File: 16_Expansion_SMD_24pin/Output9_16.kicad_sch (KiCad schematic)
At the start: 20 parts, among them J10 String10, J11 String11, J12 String12, J13 String13, J14 String14, J15 String15, J16 String16, J9 String9, U2 74HC245

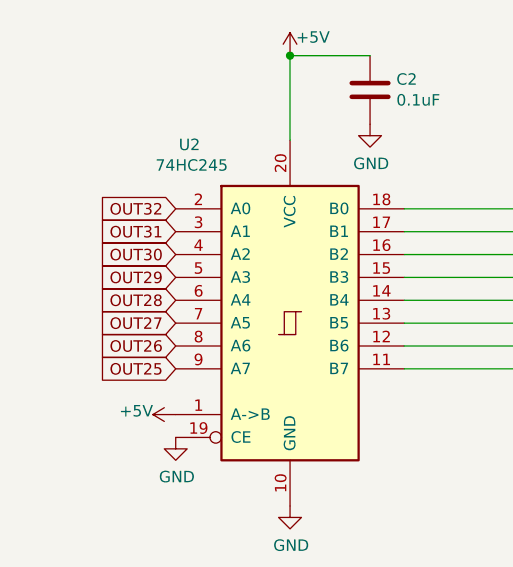
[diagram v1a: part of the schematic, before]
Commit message: added buffer resistors
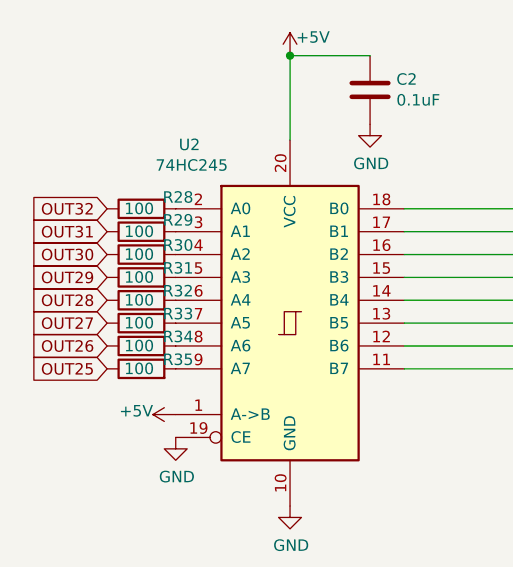
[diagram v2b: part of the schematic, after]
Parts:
- added R28, R29, R30, R31, R32, R33, R34, R35: 100, Resistor_SMD:R_0603_1608Metric_Pad0.98x0.95mm_HandSolder, symbol Device:R
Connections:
- net OUT25: now also R35.1; no longer U2.9 (A7)
- net OUT26: now also R34.1; no longer U2.8 (A6)
- net OUT27: now also R33.1; no longer U2.7 (A5)
- net OUT28: now also R32.1; no longer U2.6 (A4)
- net OUT29: now also R31.1; no longer U2.5 (A3)
- net OUT30: now also R30.1; no longer U2.4 (A2)
- net OUT31: now also R29.1; no longer U2.3 (A1)
- net OUT32: now also R28.1; no longer U2.2 (A0)
- new net: R28.2, U2.2 (A0)
- new net: R29.2, U2.3 (A1)
- new net: R30.2, U2.4 (A2)
- new net: R31.2, U2.5 (A3)
- new net: R32.2, U2.6 (A4)
- new net: R33.2, U2.7 (A5)
- new net: R34.2, U2.8 (A6)
- new net: R35.2, U2.9 (A7)
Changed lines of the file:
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@@
   (title_block
     (title "16 Expansion SMD 24pin")
-    (date "2022-06-05")
-    (rev "v2")
+    (date "2022-08-12")
+    (rev "v3")
     (company "Scott Hanson")
   )
@@
     (effects (font (size 1.27 1.27)) (justify left bottom))
   )
-  (global_label "OUT26" (shape input) (at 117.602 124.968 180) (fields_autoplaced)
+  (global_label "OUT26" (shape input) (at 109.982 124.968 180) (fields_autoplaced)
     (effects (font (size 1.27 1.27)) (justify right))
-    (property "Intersheet References" "${INTERSHEET_REFS}" (id 0) (at 0 0 0)
+    (property "Intersheet References" "${INTERSHEET_REFS}" (id 0) (at -7.62 0 0)
       (effects (font (size 1.27 1.27)) hide)
     )
@@
     )
   )
-  (global_label "OUT25" (shape input) (at 117.602 127.508 180) (fields_autoplaced)
+  (global_label "OUT25" (shape input) (at 109.982 127.508 180) (fields_autoplaced)
     (effects (font (size 1.27 1.27)) (justify right))
-    (property "Intersheet References" "${INTERSHEET_REFS}" (id 0) (at 0 0 0)
-      (effects (font (size 1.27 1.27)) hide)
-    )
-  )
-  (global_label "OUT27" (shape input) (at 117.602 122.428 180) (fields_autoplaced)
+    (property "Intersheet References" "${INTERSHEET_REFS}" (id 0) (at -7.62 0 0)
+      (effects (font (size 1.27 1.27)) hide)
+    )
+  )
+  (global_label "OUT27" (shape input) (at 109.982 122.428 180) (fields_autoplaced)
     (effects (font (size 1.27 1.27)) (justify right))
-    (property "Intersheet References" "${INTERSHEET_REFS}" (id 0) (at 0 0 0)
-      (effects (font (size 1.27 1.27)) hide)
-    )
-  )
-  (global_label "OUT28" (shape input) (at 117.602 119.888 180) (fields_autoplaced)
+    (property "Intersheet References" "${INTERSHEET_REFS}" (id 0) (at -7.62 0 0)
+      (effects (font (size 1.27 1.27)) hide)
+    )
+  )
+  (global_label "OUT28" (shape input) (at 109.982 119.888 180) (fields_autoplaced)
     (effects (font (size 1.27 1.27)) (justify right))
-    (property "Intersheet References" "${INTERSHEET_REFS}" (id 0) (at 0 0 0)
+    (property "Intersheet References" "${INTERSHEET_REFS}" (id 0) (at -7.62 0 0)
       (effects (font (size 1.27 1.27)) hide)
     )
@@
     )
   )
-  (global_label "OUT32" (shape input) (at 117.602 109.728 180) (fields_autoplaced)
+  (global_label "OUT32" (shape input) (at 109.982 109.728 180) (fields_autoplaced)
     (effects (font (size 1.27 1.27)) (justify right))
-    (property "Intersheet References" "${INTERSHEET_REFS}" (id 0) (at 0 0 0)
-      (effects (font (size 1.27 1.27)) hide)
-    )
-  )
-  (global_label "OUT31" (shape input) (at 117.602 112.268 180) (fields_autoplaced)
+    (property "Intersheet References" "${INTERSHEET_REFS}" (id 0) (at -7.62 0 0)
+      (effects (font (size 1.27 1.27)) hide)
+    )
+  )
+  (global_label "OUT31" (shape input) (at 109.982 112.268 180) (fields_autoplaced)
     (effects (font (size 1.27 1.27)) (justify right))
-    (property "Intersheet References" "${INTERSHEET_REFS}" (id 0) (at 0 0 0)
+    (property "Intersheet References" "${INTERSHEET_REFS}" (id 0) (at -7.62 0 0)
       (effects (font (size 1.27 1.27)) hide)
     )
@@
     )
   )
-  (global_label "OUT30" (shape input) (at 117.602 114.808 180) (fields_autoplaced)
+  (global_label "OUT30" (shape input) (at 109.982 114.808 180) (fields_autoplaced)
     (effects (font (size 1.27 1.27)) (justify right))
-    (property "Intersheet References" "${INTERSHEET_REFS}" (id 0) (at 0 0 0)
+    (property "Intersheet References" "${INTERSHEET_REFS}" (id 0) (at -7.62 0 0)
       (effects (font (size 1.27 1.27)) hide)
     )
@@
     )
   )
-  (global_label "OUT29" (shape input) (at 117.602 117.348 180) (fields_autoplaced)
+  (global_label "OUT29" (shape input) (at 109.982 117.348 180) (fields_autoplaced)
     (effects (font (size 1.27 1.27)) (justify right))
-    (property "Intersheet References" "${INTERSHEET_REFS}" (id 0) (at 0 0 0)
+    (property "Intersheet References" "${INTERSHEET_REFS}" (id 0) (at -7.62 0 0)
       (effects (font (size 1.27 1.27)) hide)
     )
@@
     (pin "1")
   )
+  (symbol (lib_id "Device:R") (at 113.792 119.888 90) (unit 1)
+    (in_bom yes) (on_board yes)
+    (property "Reference" "R32" (id 0) (at 117.856 118.872 90))
+    (property "Value" "100" (id 1) (at 113.538 119.888 90))
+    (property "Footprint" "Resistor_SMD:R_0603_1608Metric_Pad0.98x0.95mm_HandSolder" (id 2) (at 113.792 121.666 90)
+      (effects (font (size 1.27 1.27)) hide)
+    )
+    (property "Datasheet" "~" (id 3) (at 113.792 119.888 0)
+      (effects (font (size 1.27 1.27)) hide)
+    )
+    (pin "1")
+    (pin "2")
+  )
+  (symbol (lib_id "Device:R") (at 113.792 122.428 90) (unit 1)
+    (in_bom yes) (on_board yes)
+    (property "Reference" "R33" (id 0) (at 117.856 121.412 90))
+    (property "Value" "100" (id 1) (at 113.538 122.428 90))
+    (property "Footprint" "Resistor_SMD:R_0603_1608Metric_Pad0.98x0.95mm_HandSolder" (id 2) (at 113.792 124.206 90)
+      (effects (font (size 1.27 1.27)) hide)
+    )
+    (property "Datasheet" "~" (id 3) (at 113.792 122.428 0)
+      (effects (font (size 1.27 1.27)) hide)
+    )
+    (pin "1")
+    (pin "2")
+  )
+  (symbol (lib_id "Device:R") (at 113.792 124.968 90) (unit 1)
+    (in_bom yes) (on_board yes)
+    (property "Reference" "R34" (id 0) (at 117.856 123.952 90))
+    (property "Value" "100" (id 1) (at 113.538 124.968 90))
+    (property "Footprint" "Resistor_SMD:R_0603_1608Metric_Pad0.98x0.95mm_HandSolder" (id 2) (at 113.792 126.746 90)
+      (effects (font (size 1.27 1.27)) hide)
+    )
+    (property "Datasheet" "~" (id 3) (at 113.792 124.968 0)
+      (effects (font (size 1.27 1.27)) hide)
+    )
+    (pin "1")
+    (pin "2")
+  )
+  (symbol (lib_id "Device:R") (at 113.792 109.728 90) (unit 1)
+    (in_bom yes) (on_board yes)
+    (property "Reference" "R28" (id 0) (at 117.856 108.458 90))
+    (property "Value" "100" (id 1) (at 113.538 109.728 90))
+    (property "Footprint" "Resistor_SMD:R_0603_1608Metric_Pad0.98x0.95mm_HandSolder" (id 2) (at 113.792 111.506 90)
+      (effects (font (size 1.27 1.27)) hide)
+    )
+    (property "Datasheet" "~" (id 3) (at 113.792 109.728 0)
+      (effects (font (size 1.27 1.27)) hide)
+    )
+    (pin "1")
+    (pin "2")
+  )
+  (symbol (lib_id "Device:R") (at 113.792 114.808 90) (unit 1)
+    (in_bom yes) (on_board yes)
+    (property "Reference" "R30" (id 0) (at 117.856 113.792 90))
+    (property "Value" "100" (id 1) (at 113.538 114.808 90))
+    (property "Footprint" "Resistor_SMD:R_0603_1608Metric_Pad0.98x0.95mm_HandSolder" (id 2) (at 113.792 116.586 90)
+      (effects (font (size 1.27 1.27)) hide)
+    )
+    (property "Datasheet" "~" (id 3) (at 113.792 114.808 0)
+      (effects (font (size 1.27 1.27)) hide)
+    )
+    (pin "1")
+    (pin "2")
+  )
+  (symbol (lib_id "Device:R") (at 113.792 117.348 90) (unit 1)
+    (in_bom yes) (on_board yes)
+    (property "Reference" "R31" (id 0) (at 117.856 116.332 90))
+    (property "Value" "100" (id 1) (at 113.538 117.348 90))
+    (property "Footprint" "Resistor_SMD:R_0603_1608Metric_Pad0.98x0.95mm_HandSolder" (id 2) (at 113.792 119.126 90)
+      (effects (font (size 1.27 1.27)) hide)
+    )
+    (property "Datasheet" "~" (id 3) (at 113.792 117.348 0)
+      (effects (font (size 1.27 1.27)) hide)
+    )
+    (pin "1")
+    (pin "2")
+  )
+  (symbol (lib_id "Device:R") (at 113.792 127.508 90) (unit 1)
+    (in_bom yes) (on_board yes)
+    (property "Reference" "R35" (id 0) (at 117.856 126.492 90))
+    (property "Value" "100" (id 1) (at 113.538 127.508 90))
+    (property "Footprint" "Resistor_SMD:R_0603_1608Metric_Pad0.98x0.95mm_HandSolder" (id 2) (at 113.792 129.286 90)
+      (effects (font (size 1.27 1.27)) hide)
+    )
+    (property "Datasheet" "~" (id 3) (at 113.792 127.508 0)
+      (effects (font (size 1.27 1.27)) hide)
+    )
+    (pin "1")
+    (pin "2")
+  )
+  (symbol (lib_id "Device:R") (at 113.792 112.268 90) (unit 1)
+    (in_bom yes) (on_board yes)
+    (property "Reference" "R29" (id 0) (at 117.856 110.998 90))
+    (property "Value" "100" (id 1) (at 113.538 112.268 90))
+    (property "Footprint" "Resistor_SMD:R_0603_1608Metric_Pad0.98x0.95mm_HandSolder" (id 2) (at 113.792 114.046 90)
+      (effects (font (size 1.27 1.27)) hide)
+    )
+    (property "Datasheet" "~" (id 3) (at 113.792 112.268 0)
+      (effects (font (size 1.27 1.27)) hide)
+    )
+    (pin "1")
+    (pin "2")
+  )
 )

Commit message: update 24pin
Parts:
- removed RN3, RN4: 33, Resistor_THT:R_Array_SIP8, symbol PB_16-rescue:R_Pack04_SIP-Device
- added R12, R13, R14, R15, R16, R17, R18, R19: 33ohm, Resistor_SMD:R_0603_1608Metric, symbol Device:R_Small
- C2: footprint Capacitor_SMD:C_0805_2012Metric_Pad1.15x1.40mm_HandSolder -> Capacitor_SMD:C_0402_1005Metric
- F10, F11, F12, F13, F14, F15, F16, F9: footprint Keystone_Fuse:FUSE_3544-2 -> Scotts:FUSE_3544-2; symbol PB_16-rescue:3544-2-Keystone_Fuse -> Scotts:3544-2; LCSC (none) -> C492610
- J10, J11, J12, J13, J14, J15, J16, J9: footprint Connector_Phoenix_MC:PhoenixContact_MCV_1,5_3-G-3.5_1x03_P3.50mm_Vertical -> Scotts:PhoenixContact_MCV_3.81mm_3.5mm_1x03_Vertical
- R28, R29, R30, R31, R32, R33, R34, R35: footprint Resistor_SMD:R_0603_1608Metric_Pad0.98x0.95mm_HandSolder -> Resistor_SMD:R_0603_1608Metric
- U2: value 74HC245 -> 74HCT541; footprint Package_SO:SOIC-20W_7.5x12.8mm_P1.27mm -> Package_SO:TSSOP-20_4.4x6.5mm_P0.65mm; symbol 74xx:74HC245 -> 74xx:74HCT541; Digi-Key_PN 296-8279-1-ND -> (none); LCSC C5625 -> (none); MPN SN74HC245PWR -> (none)
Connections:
- net +5V: no longer U2.1 (A->B)
- net DOUT10: now also R13.1
- net DOUT11: now also R14.1
- net DOUT12: now also R15.1
- net DOUT13: now also R16.1
- net DOUT14: now also R17.1
- net DOUT15: now also R18.1
- net DOUT16: now also R19.1
- net DOUT9: now also R12.1
- net GND: now also U2.1 (G1)
- net at U2.15 (Y3): now also R16.2
- net at U2.16 (Y2): now also R17.2
- net at U2.17 (Y1): now also R18.2
- net at U2.18 (Y0): now also R19.2
- net at U2.11 (Y7): now also R12.2
- net at U2.12 (Y6): now also R13.2
- net at U2.13 (Y5): now also R14.2
- net at U2.14 (Y4): now also R15.2
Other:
- moved on the sheet: C2, F10, F11, F12, F13, F14, F15, F16, F9, J10, J11, J12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
